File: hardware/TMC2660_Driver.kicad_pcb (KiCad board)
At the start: 4 copper layers, 36.7 x 39.4 mm, 30 parts, among them J1 PCIe_Stepper, J2 Conn_01x04_Male, U1 TMC2660, U2 74LVC1G06, U3 24LC02

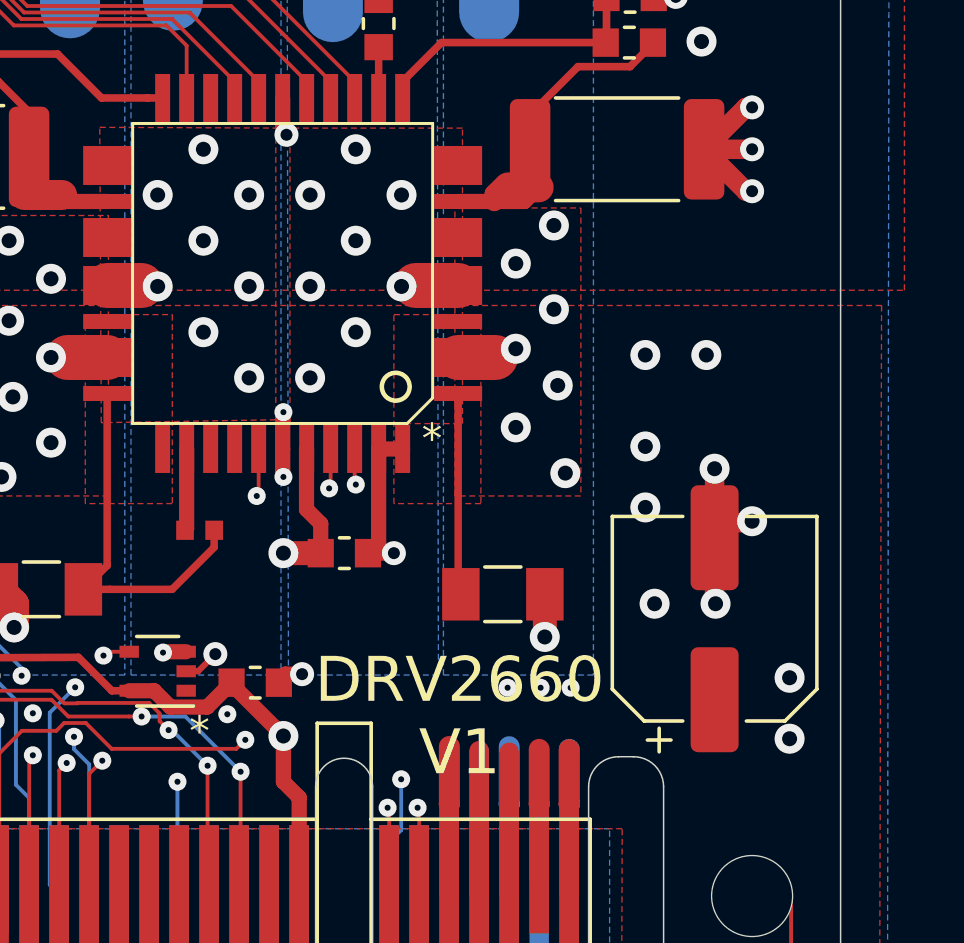
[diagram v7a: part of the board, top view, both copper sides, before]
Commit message: Update to the latest daily Kicad. Fix board outline issue on PrntrBoardV2.
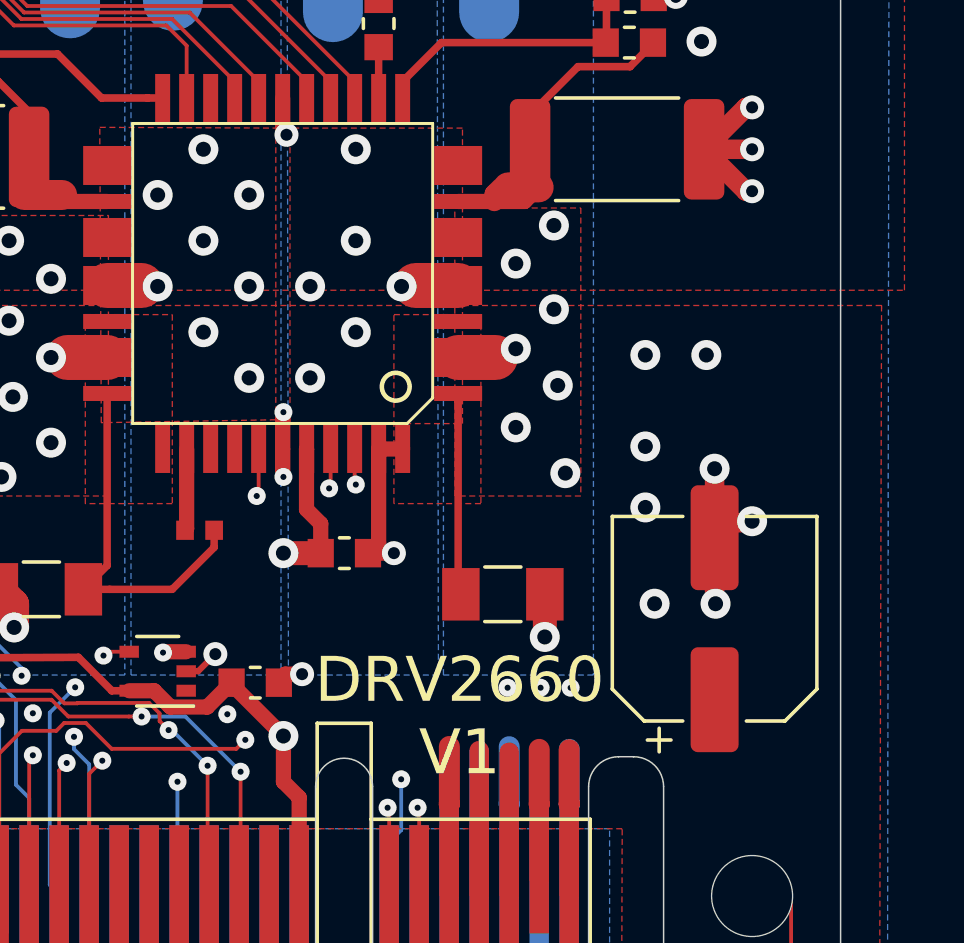
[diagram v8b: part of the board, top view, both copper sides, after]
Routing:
- net GND: vias 55 -> 53
- net /MOTA2: vias 8 -> 6
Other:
- net class Default removed
